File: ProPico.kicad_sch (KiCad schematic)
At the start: 55 parts, among them J1 USB_C_Receptacle_USB2.0, J2 SWD, J3 LEFT, J4 RIGHT, SW1 BOOTSEL, SW2 RES, U1 FM24CL16B, U2 W25Q16JVUXIQ, U3 AMS1117-3.3, U4 LM4040DBZ-3, U5 RP2040, Y1 ECS-120-12-36-AGN-TR3

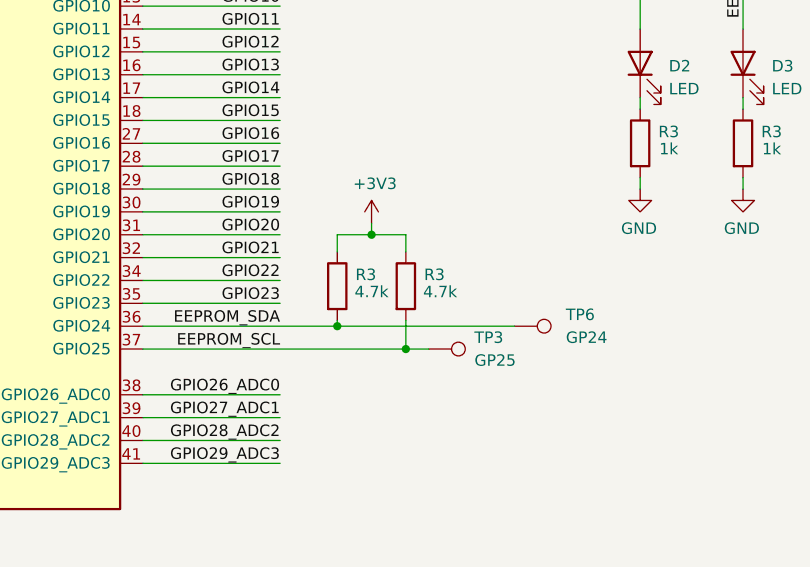
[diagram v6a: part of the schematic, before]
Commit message: added part numbers to everything in the schematic
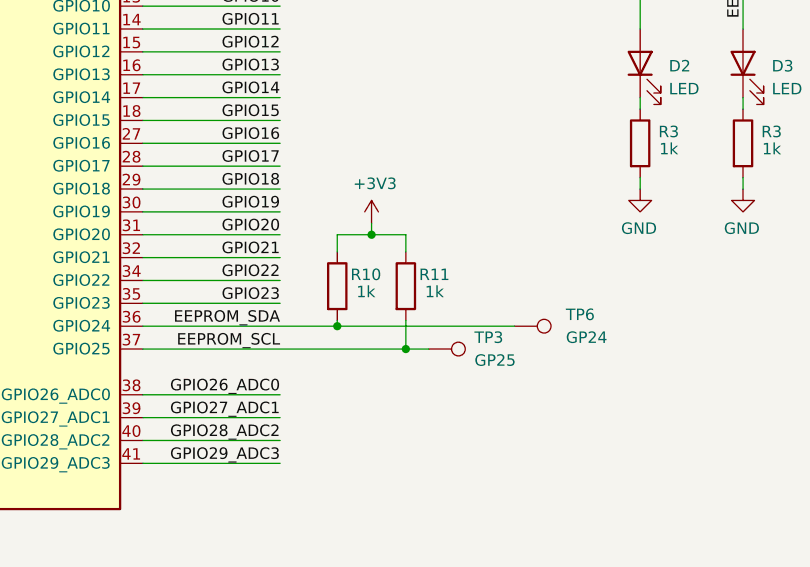
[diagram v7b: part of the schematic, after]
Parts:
- removed R3 (x2): 4.7k, Resistor_SMD:R_0402_1005Metric, symbol Device:R
- added R10, R11: 1k, Resistor_SMD:R_0402_1005Metric, symbol Device:R
- C1, C2: LCSC (none) -> C126499; P/N (none) -> GCM1555C1H180JA16D
- C11, C9: LCSC (none) -> C77009; P/N (none) -> GRM155R61E105KA12D
- C7: LCSC (none) -> C76599; P/N (none) -> C1608C0G1H103JT000N
- D2, D3: LCSC (none) -> C434425; P/N (none) -> SZYY0603O
- R1, R3: LCSC (none) -> C25543; P/N (none) -> 0402WGJ0102TCE
- R4, R5: LCSC (none) -> C2909343; P/N (none) -> FRC0402F27R0TS
- R7: LCSC (none) -> C22808; P/N (none) -> 0603WAF1500T5E
- U4: LCSC (none) -> C460726; P/N (none) -> LM4040D30FTA
- U5: LCSC (none) -> C2040; P/N (none) -> RP2040
- Y1: LCSC (none) -> C284155; P/N (none) -> TXM12M0004252FBCEO00T
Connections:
- net +3V3: now also R10.1, R11.1
- net EEPROM_SCL: now also R11.2
- net EEPROM_SDA: now also R10.2
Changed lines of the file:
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@@
+      (effects (font (size 1.27 1.27)) hide)
+    )
+    (property "LCSC" "C434425" (at 346.71 125.095 90)
+      (effects (font (size 1.27 1.27)) hide)
+    )
+    (property "P/N" "SZYY0603O" (at 346.71 125.095 90)
       (effects (font (size 1.27 1.27)) hide)
     )
@@
     )
     (property "Datasheet" "~" (at 120.65 140.97 0)
+      (effects (font (size 1.27 1.27)) hide)
+    )
+    (property "LCSC" "C284155" (at 120.65 140.97 90)
+      (effects (font (size 1.27 1.27)) hide)
+    )
+    (property "P/N" "TXM12M0004252FBCEO00T" (at 120.65 140.97 90)
       (effects (font (size 1.27 1.27)) hide)
     )
@@
     )
     (property "Datasheet" "~" (at 230.505 62.865 0)
+      (effects (font (size 1.27 1.27)) hide)
+    )
+    (property "LCSC" "C77009" (at 230.505 62.865 0)
+      (effects (font (size 1.27 1.27)) hide)
+    )
+    (property "P/N" "GRM155R61E105KA12D" (at 230.505 62.865 0)
       (effects (font (size 1.27 1.27)) hide)
     )
@@
     )
     (property "Datasheet" "" (at 240.665 126.365 0)
+      (effects (font (size 1.27 1.27)) hide)
+    )
+    (property "LCSC" "C2040" (at 259.715 126.365 0)
+      (effects (font (size 1.27 1.27)) hide)
+    )
+    (property "P/N" "RP2040" (at 259.715 126.365 0)
       (effects (font (size 1.27 1.27)) hide)
     )
@@
       (effects (font (size 1.27 1.27)) hide)
     )
+    (property "LCSC" "C76599" (at 106.68 192.405 0)
+      (effects (font (size 1.27 1.27)) hide)
+    )
+    (property "P/N" "C1608C0G1H103JT000N" (at 106.68 192.405 0)
+      (effects (font (size 1.27 1.27)) hide)
+    )
     (pin "1")
     (pin "2")
@@
     )
     (property "Datasheet" "~" (at 35.56 100.33 0)
+      (effects (font (size 1.27 1.27)) hide)
+    )
+    (property "LCSC" "C25543" (at 35.56 100.33 0)
+      (effects (font (size 1.27 1.27)) hide)
+    )
+    (property "P/N" "0402WGJ0102TCE" (at 35.56 100.33 0)
       (effects (font (size 1.27 1.27)) hide)
     )
@@
       (effects (font (size 1.27 1.27)) hide)
     )
+    (property "LCSC" "C77009" (at 285.115 62.865 0)
+      (effects (font (size 1.27 1.27)) hide)
+    )
+    (property "P/N" "GRM155R61E105KA12D" (at 285.115 62.865 0)
+      (effects (font (size 1.27 1.27)) hide)
+    )
     (pin "1")
     (pin "2")
@@
     )
     (property "Datasheet" "~" (at 306.705 85.725 0)
+      (effects (font (size 1.27 1.27)) hide)
+    )
+    (property "LCSC" "C2909343" (at 306.705 85.725 90)
+      (effects (font (size 1.27 1.27)) hide)
+    )
+    (property "P/N" "FRC0402F27R0TS" (at 306.705 85.725 90)
       (effects (font (size 1.27 1.27)) hide)
     )
@@
     )
   )
+  (symbol (lib_id "Device:R") (at 320.675 149.86 0) (unit 1)
+    (in_bom yes) (on_board yes) (dnp no)
+    (property "Reference" "R11" (at 323.85 148.59 0)
+      (effects (font (size 1.27 1.27)))
+    )
+    (property "Value" "1k" (at 323.85 150.495 0)
+      (effects (font (size 1.27 1.27)))
+    )
+    (property "Footprint" "Resistor_SMD:R_0402_1005Metric" (at 318.897 149.86 90)
+      (effects (font (size 1.27 1.27)) hide)
+    )
+    (property "Datasheet" "~" (at 320.675 149.86 0)
+      (effects (font (size 1.27 1.27)) hide)
+    )
+    (property "LCSC" "C25543" (at 320.675 149.86 0)
+      (effects (font (size 1.27 1.27)) hide)
+    )
+    (property "P/N" "0402WGJ0102TCE" (at 320.675 149.86 0)
+      (effects (font (size 1.27 1.27)) hide)
+    )
+    (pin "1")
+    (pin "2")
+    (instances
+      (project "ProPico"
+        (path "/73e46140-01b8-4ec1-93bb-0d72bea0e0ee"
+          (reference "R11") (unit 1)
+        )
+      )
+    )
+  )
   (symbol (lib_id "Connector_Generic:Conn_01x04") (at 195.58 160.655 0) (mirror y) (unit 1)
     (in_bom yes) (on_board yes) (dnp no)
@@
     )
     (property "Datasheet" "~" (at 346.71 133.985 0)
+      (effects (font (size 1.27 1.27)) hide)
+    )
+    (property "LCSC" "C25543" (at 346.71 133.985 0)
+      (effects (font (size 1.27 1.27)) hide)
+    )
+    (property "P/N" "0402WGJ0102TCE" (at 346.71 133.985 0)
       (effects (font (size 1.27 1.27)) hide)
     )
@@
       (effects (font (size 1.27 1.27)) hide)
     )
+    (property "LCSC" "C22808" (at 126.365 175.26 0)
+      (effects (font (size 1.27 1.27)) hide)
+    )
+    (property "P/N" "0603WAF1500T5E" (at 126.365 175.26 0)
+      (effects (font (size 1.27 1.27)) hide)
+    )
     (pin "1")
     (pin "2")
@@
     )
   )
-  (symbol (lib_id "Device:R") (at 320.675 149.86 0) (unit 1)
-    (in_bom yes) (on_board yes) (dnp no)
-    (property "Reference" "R3" (at 323.85 148.59 0)
-      (effects (font (size 1.27 1.27)))
-    )
-    (property "Value" "4.7k" (at 324.485 150.495 0)
-      (effects (font (size 1.27 1.27)))
-    )
-    (property "Footprint" "Resistor_SMD:R_0402_1005Metric" (at 318.897 149.86 90)
-      (effects (font (size 1.27 1.27)) hide)
-    )
-    (property "Datasheet" "~" (at 320.675 149.86 0)
-      (effects (font (size 1.27 1.27)) hide)
-    )
-    (pin "1")
-    (pin "2")
-    (instances
-      (project "rpcube"
-        (path "/2fe78bb3-6c9b-4737-8793-454e476eabbd"
-          (reference "R3") (unit 1)
-        )
-      )
-      (project "ProPico"
-        (path "/73e46140-01b8-4ec1-93bb-0d72bea0e0ee"
-          (reference "R11") (unit 1)
-        )
-      )
-    )
-  )
   (symbol (lib_id "Device:R") (at 306.705 83.185 270) (unit 1)
     (in_bom yes) (on_board yes) (dnp no)
@@
     )
     (property "Datasheet" "~" (at 306.705 83.185 0)
+      (effects (font (size 1.27 1.27)) hide)
+    )
+    (property "LCSC" "C2909343" (at 306.705 83.185 90)
+      (effects (font (size 1.27 1.27)) hide)
+    )
+    (property "P/N" "FRC0402F27R0TS" (at 306.705 83.185 90)
       (effects (font (size 1.27 1.27)) hide)
     )
@@
       (effects (font (size 1.27 1.27) italic) hide)
     )
+    (property "LCSC" "C460726" (at 126.365 193.04 90)
+      (effects (font (size 1.27 1.27)) hide)
+    )
+    (property "P/N" "LM4040D30FTA" (at 126.365 193.04 90)
+      (effects (font (size 1.27 1.27)) hide)
+    )
     (pin "1")
     (pin "2")
@@
       (effects (font (size 1.27 1.27)) hide)
     )
+    (property "LCSC" "C25543" (at 358.14 133.985 0)
+      (effects (font (size 1.27 1.27)) hide)
+    )
+    (property "P/N" "0402WGJ0102TCE" (at 358.14 133.985 0)
+      (effects (font (size 1.27 1.27)) hide)
+    )
     (pin "1")
     (pin "2")
@@
     )
   )
-  (symbol (lib_id "Device:R") (at 313.055 149.86 0) (unit 1)
-    (in_bom yes) (on_board yes) (dnp no)
-    (property "Reference" "R3" (at 316.23 148.59 0)
-      (effects (font (size 1.27 1.27)))
-    )
-    (property "Value" "4.7k" (at 316.865 150.495 0)
-      (effects (font (size 1.27 1.27)))
-    )
-    (property "Footprint" "Resistor_SMD:R_0402_1005Metric" (at 311.277 149.86 90)
-      (effects (font (size 1.27 1.27)) hide)
-    )
-    (property "Datasheet" "~" (at 313.055 149.86 0)
-      (effects (font (size 1.27 1.27)) hide)
-    )
-    (pin "1")
-    (pin "2")
-    (instances
-      (project "rpcube"
-        (path "/2fe78bb3-6c9b-4737-8793-454e476eabbd"
-          (reference "R3") (unit 1)
-        )
-      )
-      (project "ProPico"
-        (path "/73e46140-01b8-4ec1-93bb-0d72bea0e0ee"
-          (reference "R10") (unit 1)
-        )
-      )
-    )
-  )
   (symbol (lib_id "power:GND") (at 230.505 67.945 0) (unit 1)
     (in_bom yes) (on_board yes) (dnp no)
@@
     )
     (property "Datasheet" "~" (at 105.41 146.05 0)
+      (effects (font (size 1.27 1.27)) hide)
+    )
+    (property "LCSC" "C126499" (at 105.41 146.05 90)
+      (effects (font (size 1.27 1.27)) hide)
+    )
+    (property "P/N" "GCM1555C1H180JA16D" (at 105.41 146.05 90)
       (effects (font (size 1.27 1.27)) hide)
     )
@@
     )
     (property "Datasheet" "~" (at 358.14 125.095 0)
+      (effects (font (size 1.27 1.27)) hide)
+    )
+    (property "LCSC" "C434425" (at 358.14 125.095 90)
+      (effects (font (size 1.27 1.27)) hide)
+    )
+    (property "P/N" "SZYY0603O" (at 358.14 125.095 90)
       (effects (font (size 1.27 1.27)) hide)
     )
@@
       (effects (font (size 1.27 1.27)) hide)
     )
+    (property "LCSC" "C126499" (at 105.41 135.89 90)
+      (effects (font (size 1.27 1.27)) hide)
+    )
+    (property "P/N" "GCM1555C1H180JA16D" (at 105.41 135.89 90)
+      (effects (font (size 1.27 1.27)) hide)
+    )
     (pin "1")
     (pin "2")
@@
         )
       )
+    )
+  )
+  (symbol (lib_id "Device:R") (at 313.055 149.86 0) (unit 1)
+    (in_bom yes) (on_board yes) (dnp no)
+    (property "Reference" "R10" (at 316.23 148.59 0)
+      (effects (font (size 1.27 1.27)))
+    )
+    (property "Value" "1k" (at 316.23 150.495 0)
+      (effects (font (size 1.27 1.27)))
+    )
+    (property "Footprint" "Resistor_SMD:R_0402_1005Metric" (at 311.277 149.86 90)
+      (effects (font (size 1.27 1.27)) hide)
+    )
+    (property "Datasheet" "~" (at 313.055 149.86 0)
+      (effects (font (size 1.27 1.27)) hide)
+    )
+    (property "LCSC" "C25543" (at 313.055 149.86 0)
+      (effects (font (size 1.27 1.27)) hide)
+    )
+    (property "P/N" "0402WGJ0102TCE" (at 313.055 149.86 0)
+      (effects (font (size 1.27 1.27)) hide)
+    )
+    (pin "1")
+    (pin "2")
+    (instances
+      (project "ProPico"
+        (path "/73e46140-01b8-4ec1-93bb-0d72bea0e0ee"
+          (reference "R10") (unit 1)
+        )
+      )

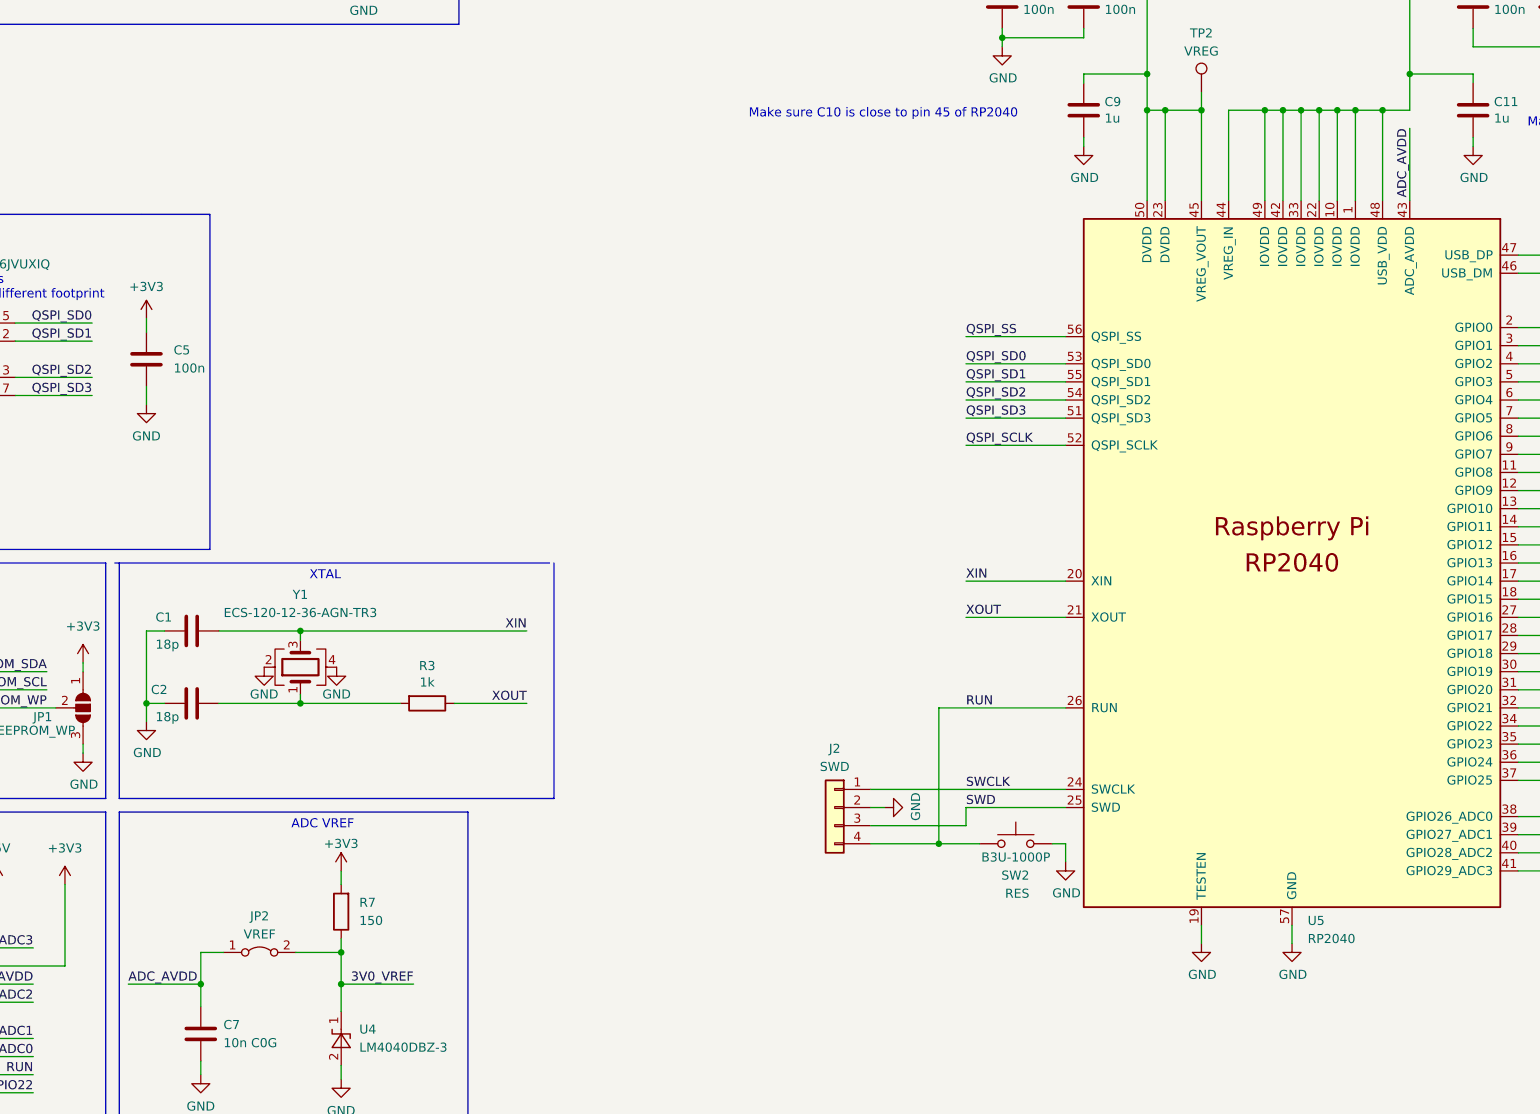
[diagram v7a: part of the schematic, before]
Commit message: changed the names of some nets to be more logical
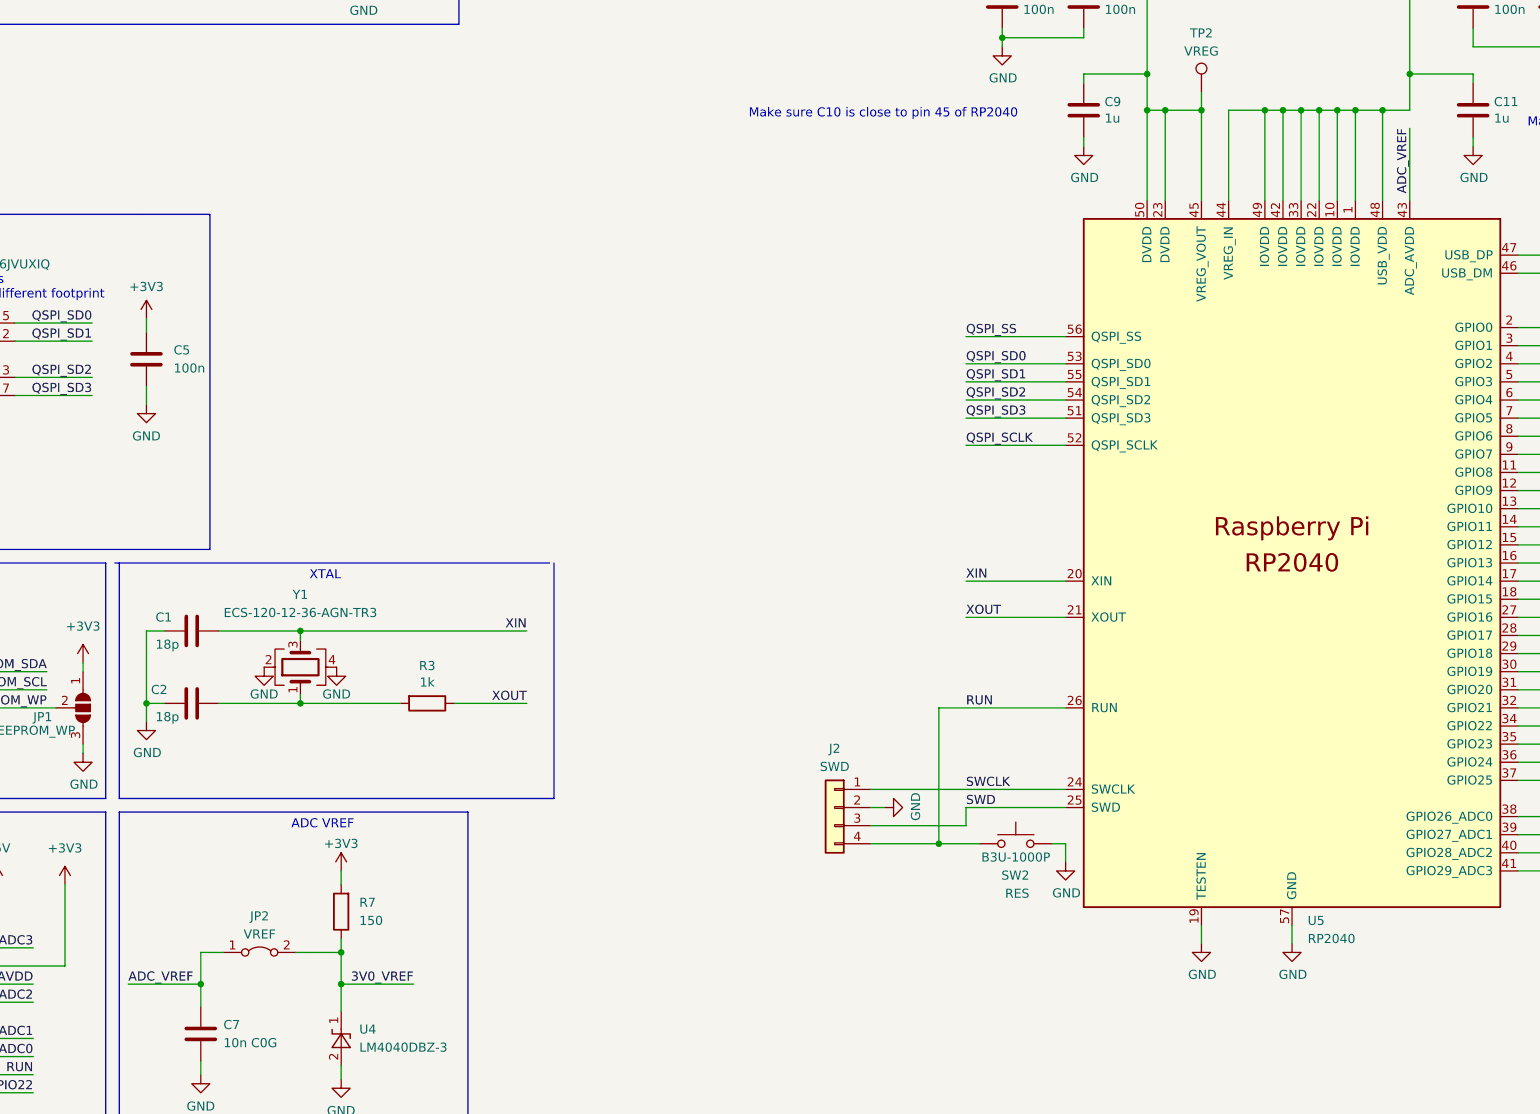
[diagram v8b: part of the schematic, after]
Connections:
- net ADC_AVDD: no longer C7.1, JP2.1 (A), U5.43 (ADC_AVDD)
- new net ADC_VREF: C7.1, JP2.1 (A), U5.43 (ADC_AVDD)
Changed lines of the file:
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@@
     (effects (font (size 1.27 1.27)) (justify left bottom))
   )
-  (label "ADC_AVDD" (at 276.225 65.405 270) (fields_autoplaced)
+  (label "ADC_VREF" (at 276.225 65.405 270) (fields_autoplaced)
     (effects (font (size 1.27 1.27)) (justify right bottom))
   )
@@
     (effects (font (size 1.27 1.27)) (justify left bottom))
   )
-  (label "ADC_AVDD" (at 96.52 185.42 0) (fields_autoplaced)
+  (label "ADC_VREF" (at 96.52 185.42 0) (fields_autoplaced)
     (effects (font (size 1.27 1.27)) (justify left bottom))
   )
